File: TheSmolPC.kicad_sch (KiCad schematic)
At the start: 79 parts, among them J1 USB_C_Receptacle_USB2.0_16P, J2 USB_A, J3 USB_A, J4 HDMI_A, J5 Micro_SD_Card_Det2, J6 Conn_01x04, J7 Conn_01x03, J8 AudioJack4_Ground, SW1 SW_Push, U1 RP2350B-QFN80, U2 CH334R, U3 TPS63000, U4 W25Q128JVS, U5 APS6404L-SQRx-SN, U6 TXS0102DQE, U7 ESP32-C6-MINI-1, U8 PCM5101A, Y1 12MHz, Y2 12MHz

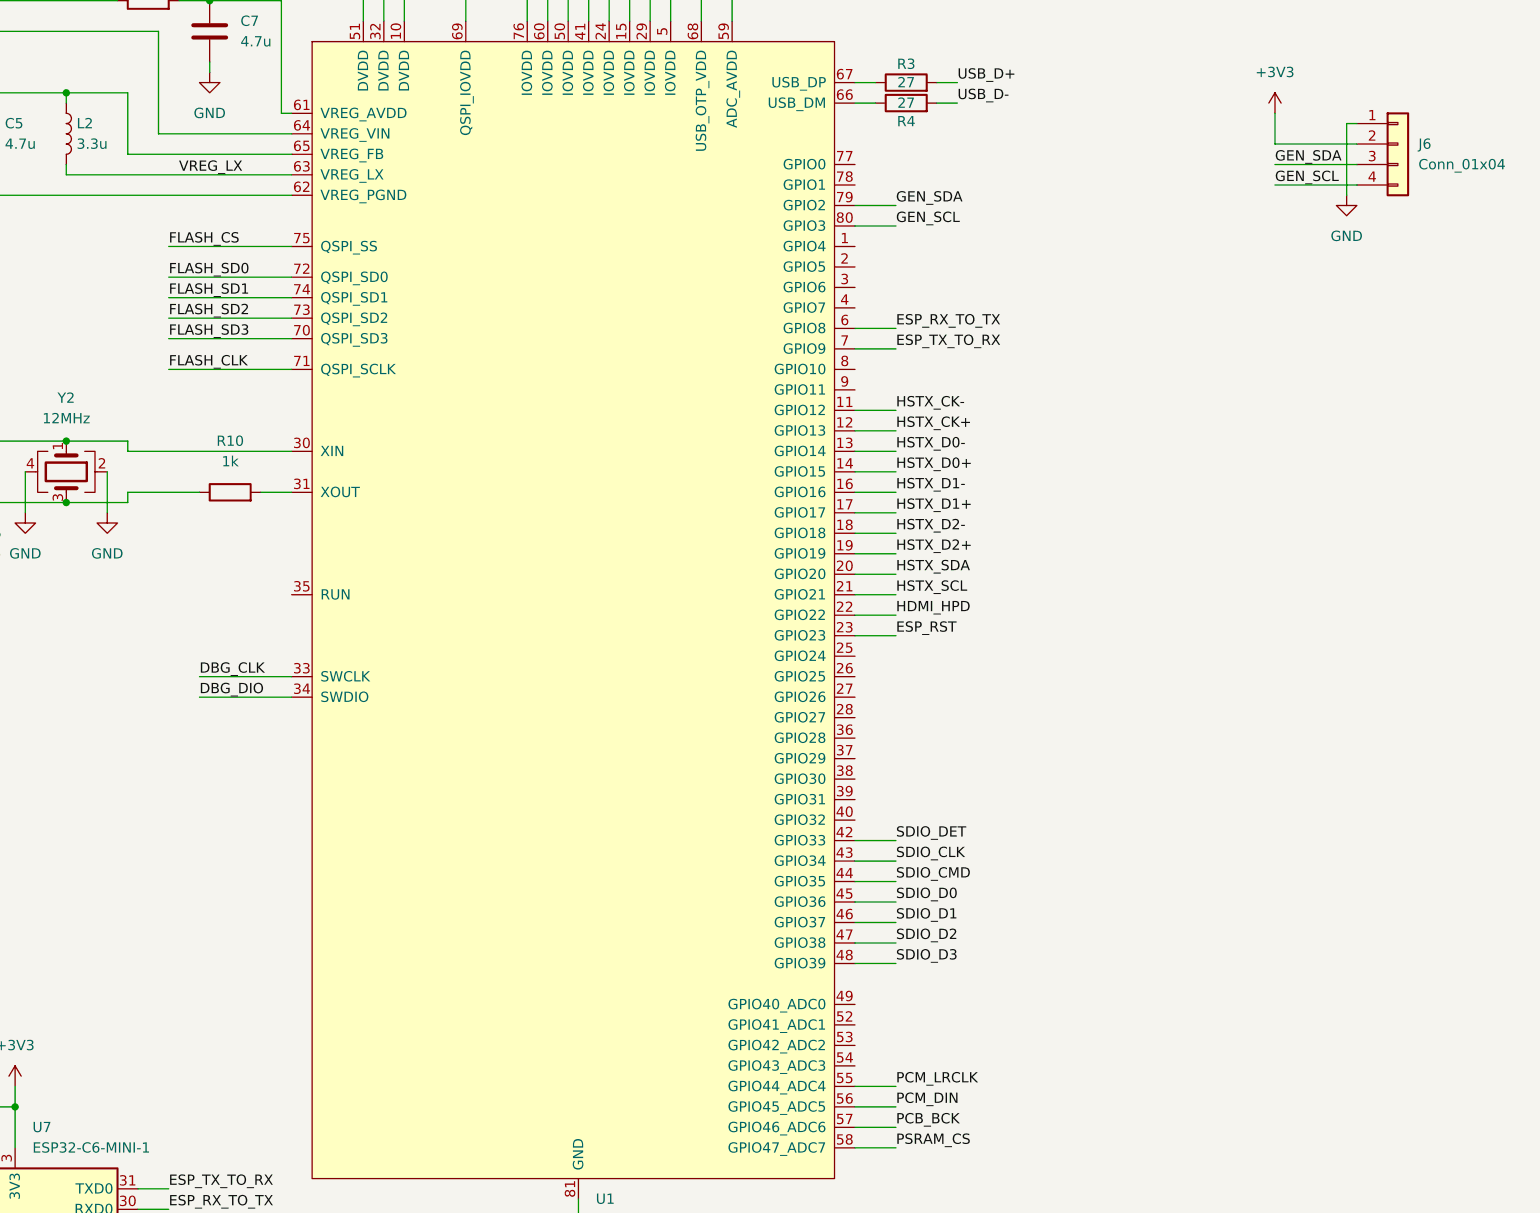
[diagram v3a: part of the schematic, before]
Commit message: finalizing schema (some still wip and will be changed dynamically
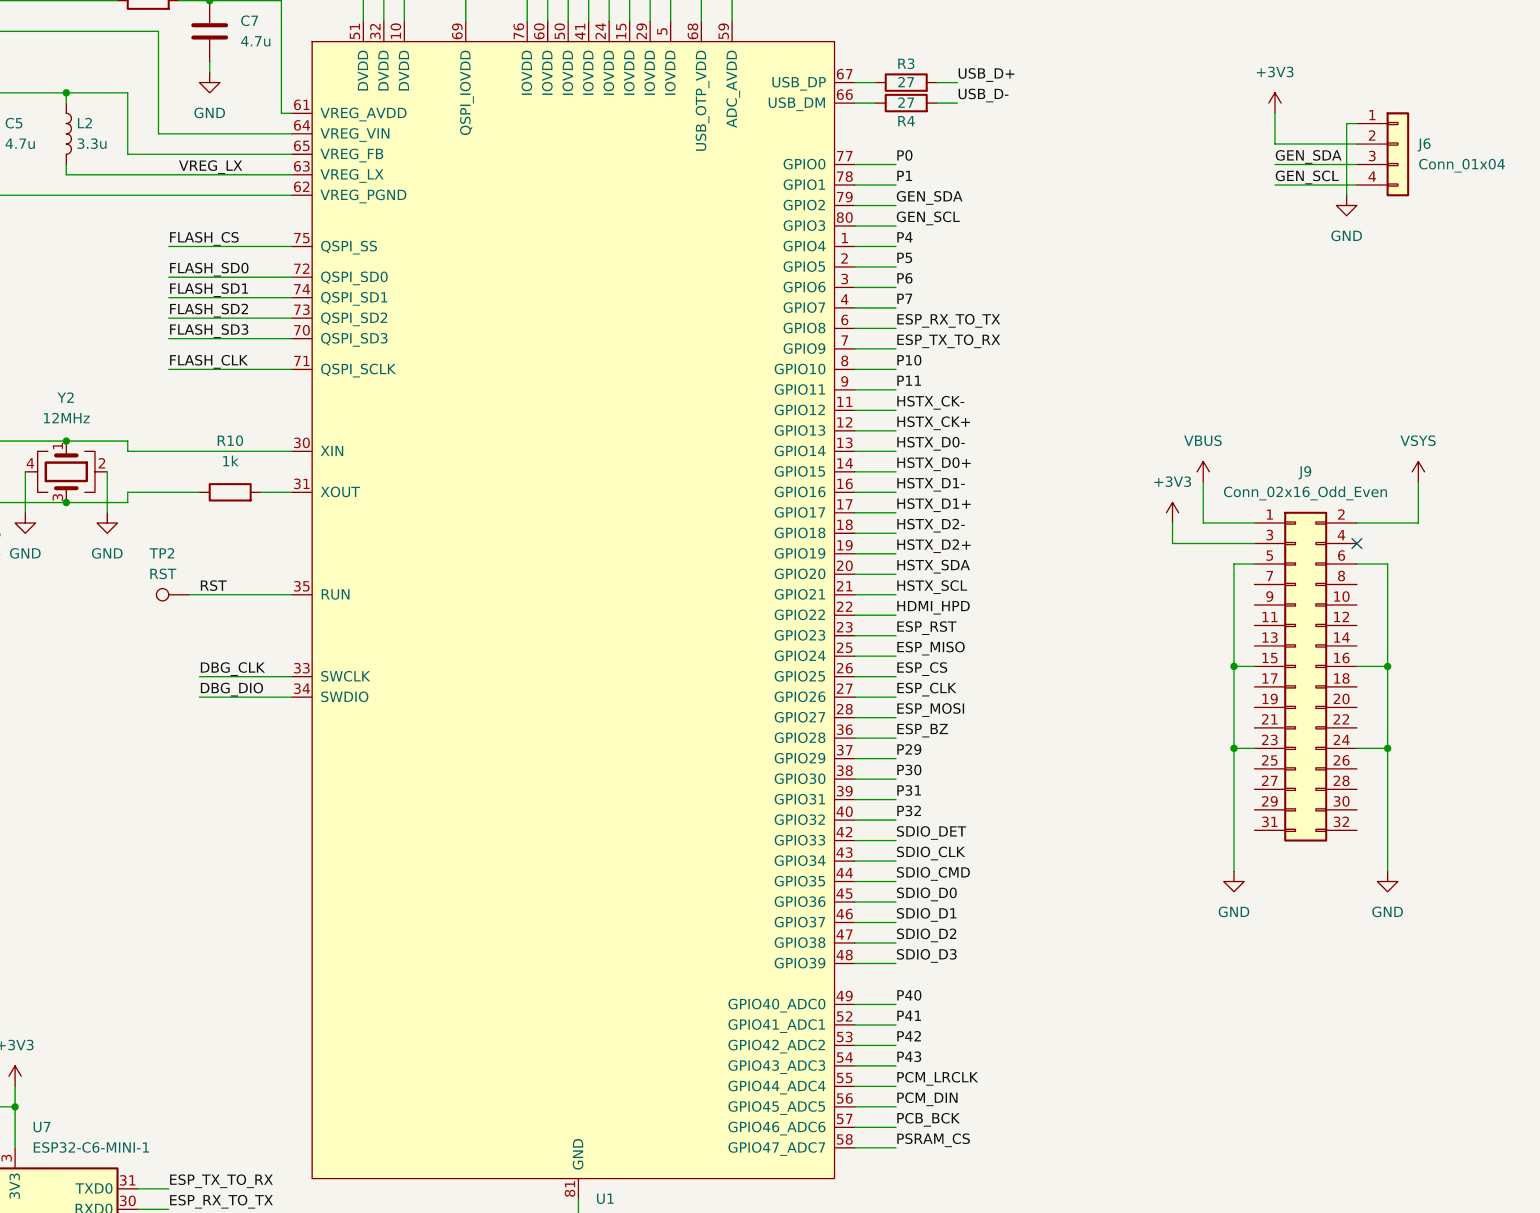
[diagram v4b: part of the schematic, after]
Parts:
- added J9: Conn_02x16_Odd_Even, Connector_PinHeader_2.54mm:PinHeader_2x16_P2.54mm_Vertical_SMD, symbol Connector_Generic:Conn_02x16_Odd_Even
- added TP2: RST, TestPoint:TestPoint_Pad_D1.0mm, symbol Connector:TestPoint
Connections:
- net +3V3: now also J9.3 (Pin_3)
- net ESP_BZ: now also U1.36 (GPIO28)
- net ESP_CLK: now also U1.27 (GPIO26)
- net ESP_CS: now also U1.26 (GPIO25)
- net ESP_MISO: now also U1.25 (GPIO24)
- net ESP_MOSI: now also U1.28 (GPIO27)
- net GND: now also J9.15 (Pin_15), J9.16 (Pin_16), J9.23 (Pin_23), J9.24 (Pin_24), J9.5 (Pin_5), J9.6 (Pin_6)
- net VBUS: now also J9.1 (Pin_1)
- net VSYS: now also J9.2 (Pin_2)
- net P4: now reaches U1.1 (GPIO4)
- net P5: now reaches U1.2 (GPIO5)
- net P6: now reaches U1.3 (GPIO6)
- net RST: now reaches U1.35 (RUN)
- net RST: now also TP2.1
- net P29: now reaches U1.37 (GPIO29)
- net P30: now reaches U1.38 (GPIO30)
- net P31: now reaches U1.39 (GPIO31)
- net P7: now reaches U1.4 (GPIO7)
- net P32: now reaches U1.40 (GPIO32)
- net P40: now reaches U1.49 (GPIO40_ADC0)
- net P41: now reaches U1.52 (GPIO41_ADC1)
- net P42: now reaches U1.53 (GPIO42_ADC2)
- net P43: now reaches U1.54 (GPIO43_ADC3)
- net P0: now reaches U1.77 (GPIO0)
- net P1: now reaches U1.78 (GPIO1)
- net P10: now reaches U1.8 (GPIO10)
- net P11: now reaches U1.9 (GPIO11)
- no-connect marks 23 -> 24

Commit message: pcb finally finished
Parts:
- removed J9: Conn_02x16_Odd_Even, Connector_PinHeader_2.54mm:PinHeader_2x16_P2.54mm_Vertical_SMD, symbol Connector_Generic:Conn_02x16_Odd_Even
- added C37, C38: 2.2u, Capacitor_SMD:C_0402_1005Metric, symbol Device:C
- added C39, C40: 1u, Capacitor_SMD:C_0402_1005Metric, symbol Device:C
- added D2: GREEN, LED_SMD:LED_0402_1005Metric, symbol Device:LED
- added D3: RED, LED_SMD:LED_0402_1005Metric, symbol Device:LED
- added H1, H2, H3, H4: MountingHole_Pad, MountingHole:MountingHole_3.2mm_M3_DIN965_Pad, symbol Mechanical:MountingHole_Pad
- added J10, J11, J9: Conn_01x04, Connector_JST:JST_SH_SM04B-SRSS-TB_1x04-1MP_P1.00mm_Horizontal, symbol Connector_Generic:Conn_01x04
- added R17, R18: 470, Resistor_SMD:R_0402_1005Metric, symbol Device:R
- added R19: 1k, Resistor_SMD:R_0402_1005Metric, symbol Device:R
- added R20, R21: 330, Resistor_SMD:R_0402_1005Metric, symbol Device:R
- added U9: TLV70033_SOT353, Package_TO_SOT_SMD:SOT-353_SC-70-5, symbol Regulator_Linear:TLV70033_SOT353
- C13, C14: footprint Capacitor_SMD:C_0402_1005Metric -> Capacitor_SMD:C_0805_2012Metric
- C15: footprint Capacitor_SMD:C_0402_1005Metric -> Capacitor_SMD:C_0805_2012Metric; now not fitted; now left out of the parts list
- J8: footprint Connector_Audio:Jack_3.5mm_CUI_SJ1-3515N_Horizontal -> Connector_Audio:Jack_3.5mm_KoreanHropartsElec_PJ-320D-4A_Horizontal
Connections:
- net +1V1: no longer U1.69 (QSPI_IOVDD)
- net +3.3VA: now also C40.1, U9.5 (OUT)
- net +3V3: now also U1.69 (QSPI_IOVDD), J10.2 (Pin_2), J11.2 (Pin_2), J9.2 (Pin_2), R21.1
- net AUX_OUTL: now also C37.1, R17.2; no longer U8.6 (OUTL)
- net AUX_OUTR: now also C38.1, R18.2; no longer U8.7 (OUTR)
- net FLASH_CS: now also R19.2; no longer SW1.2
- net GEN_SCL: now also J10.4 (Pin_4), J11.4 (Pin_4), J9.4 (Pin_4)
- net GEN_SDA: now also J10.3 (Pin_3), J11.3 (Pin_3), J9.3 (Pin_3)
- net GND: now also C37.2, C38.2, C39.2, C40.2, D2.1 (K), D3.1 (K), H1.1, H2.1, H3.1, H4.1, J10.1 (Pin_1), J11.1 (Pin_1), J9.1 (Pin_1), U9.2 (GND)
- net P10: now also R20.1
- net VSYS: now also C39.1, U9.1 (IN), U9.3 (EN)
- net MCU_D-: now reaches R4.1, U1.66 (USB_DM)
- net MCU_D+: now reaches R3.1, U1.67 (USB_DP)
- new net: D3.2 (A), R21.2
- new net: R17.1, U8.6 (OUTL)
- new net: R18.1, U8.7 (OUTR)
- new net: D2.2 (A), R20.2
- new net: R19.1, SW1.2
- no-connect marks 24 -> 23
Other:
- moved on the sheet: R3, R4, SW1
